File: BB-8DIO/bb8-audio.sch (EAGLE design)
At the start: 27 parts, among them IC1 7805L, IC3 74LS125N

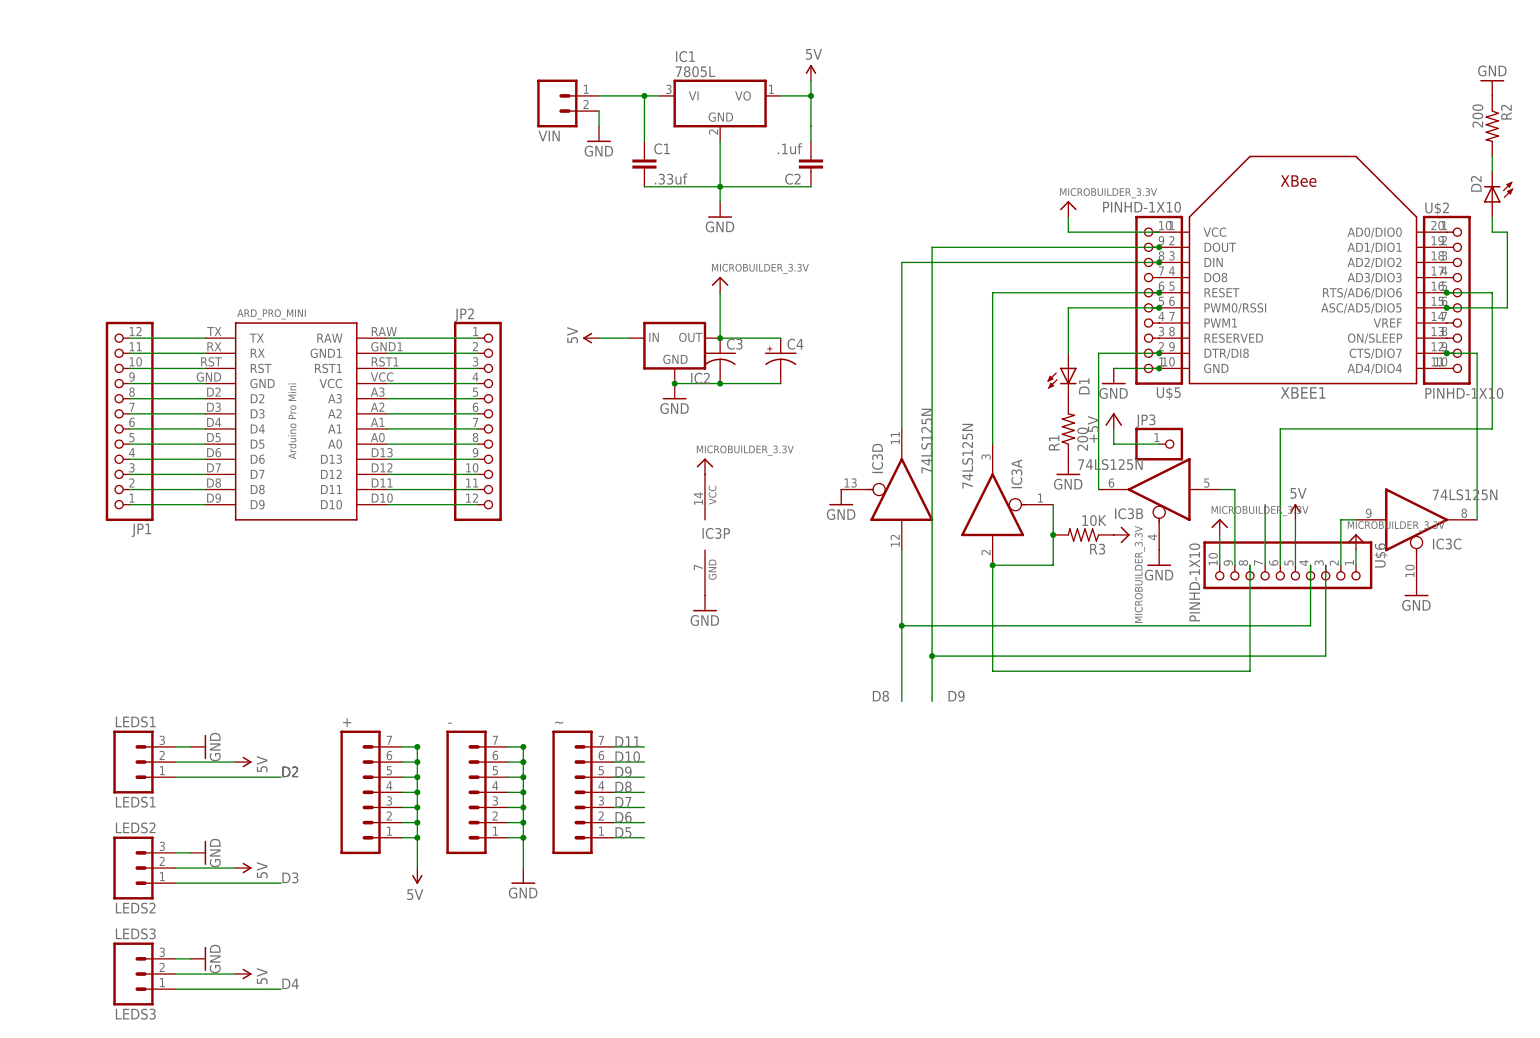
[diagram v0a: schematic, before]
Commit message: Revision 0.3 of the BB-8DIO board.
Adding revision 0.3. This has the audio breakout board footprint so the
breakout can be dropped on using header pins. This also has reworked a
lot of other pins and headers have been removed because they are no
longer available after adding the audio breakout. Resolved some
silkscreen issues and also resolved issues with 5V on arduino input and
Xbee input.
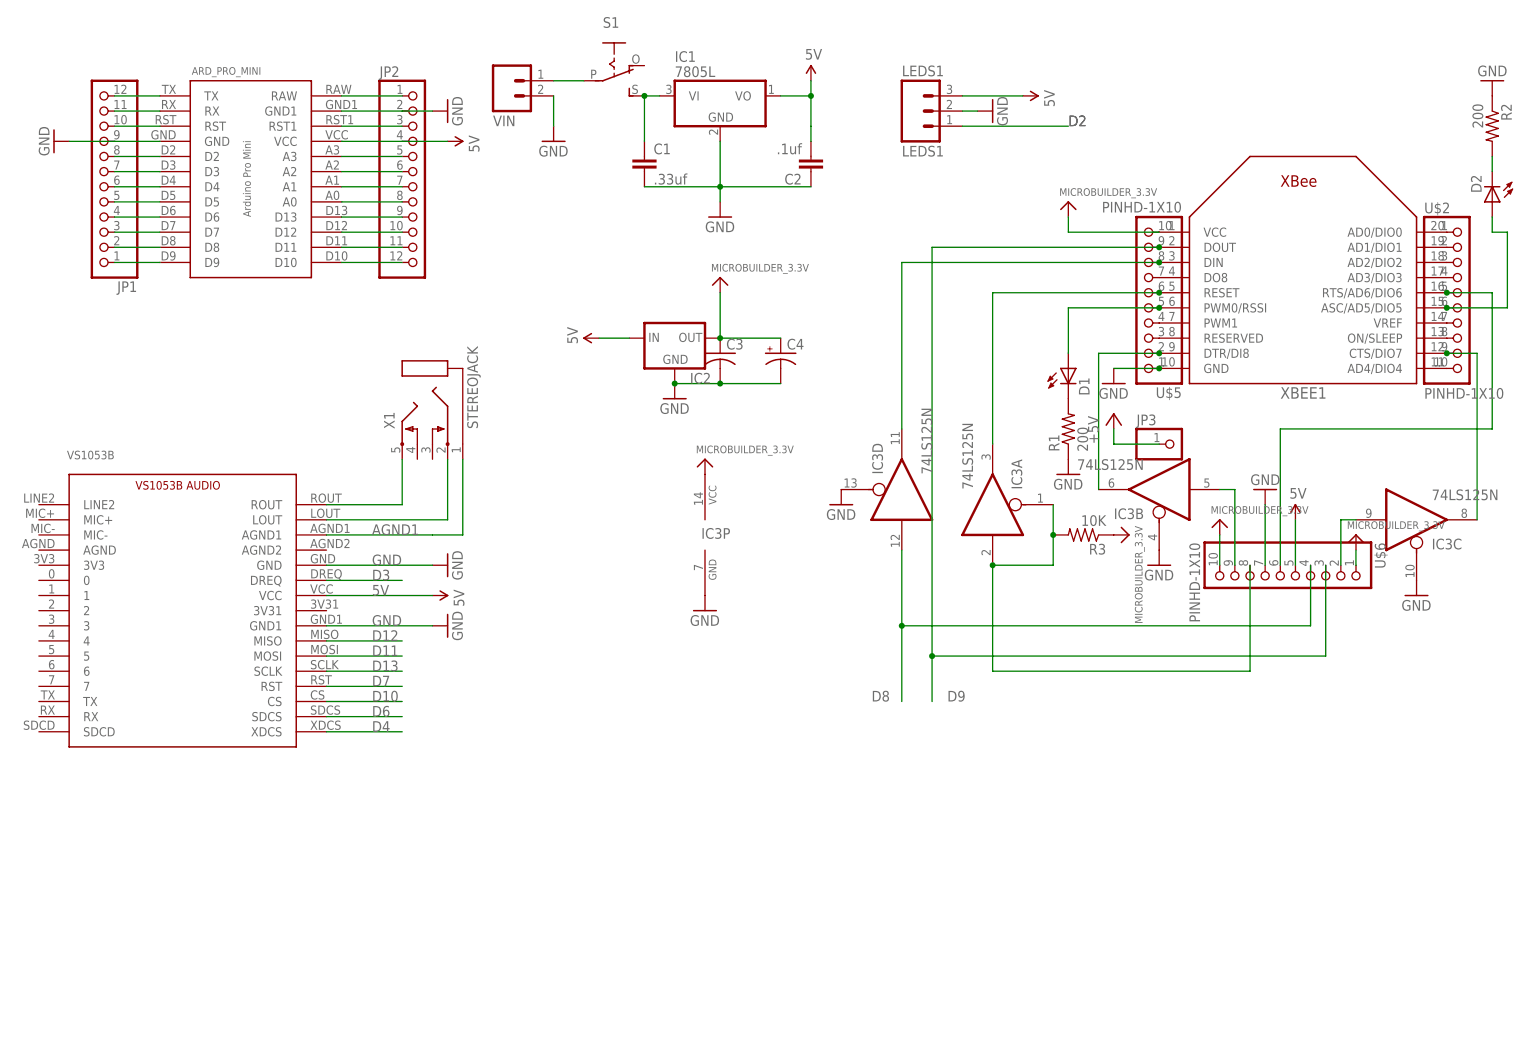
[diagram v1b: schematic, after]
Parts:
- removed +, -, ~: (no value), SparkFun-Connectors:M07
- removed LEDS2: LEDS2, SparkFun-Connectors:M03PTH
- removed LEDS3: LEDS3, SparkFun-Connectors:M03PTH
- added S1: (no value), adafruit:EG1218S
- added VS1053B: VS1053B_BREAKOUT, VS1053B_BREAKOUT:VS1053B_BREAKOUT
- added X1: STEREOJACK, adafruit:STEREOJACK
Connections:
- removed net VCC: ARD_PRO_MINI.VCC, JP2.4
- new net AGND1: VS1053B.AGND1, X1.1
- new net N$25: VS1053B.ROUT, X1.5
- new net N$26: S1.P, VIN.1
- net 5V: now also ARD_PRO_MINI.VCC, JP2.4, LEDS1.3, VS1053B.VCC; no longer +.1, +.2, +.3, +.4, +.5, +.6, +.7, LEDS1.2, LEDS2.2, LEDS3.2
- net D10: now also VS1053B.CS; no longer ~.6
- net D11: now also VS1053B.MOSI; no longer ~.7
- net D12: now also VS1053B.MISO
- net D13: now also VS1053B.SCLK
- net D3: now also VS1053B.DREQ; no longer LEDS2.1
- net D4: now also VS1053B.XDCS; no longer LEDS3.1
- net D5: no longer ~.1
- net D6: now also VS1053B.SDCS; no longer ~.2
- net D7: now also VS1053B.RST; no longer ~.3
- net D8: no longer ~.4
- net D9: no longer ~.5
- net GND: now also LEDS1.2, U$6.7, VS1053B.GND, VS1053B.GND1; no longer -.1, -.2, -.3, -.4, -.5, -.6, -.7, LEDS1.3, LEDS2.3, LEDS3.3
- net N$2: now also S1.S; no longer VIN.1
- net N$21: now also VS1053B.LOUT, X1.2; no longer U$6.7
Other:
- moved on the sheet: ARD_PRO_MINI, JP1, JP2, LEDS1, VIN
